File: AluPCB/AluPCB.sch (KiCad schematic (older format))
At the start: 83 parts, among them J1 CON_U, J2 CON_U, J3 CON_U, J4 GND, J5 VIN, Q1 AON6276, Q2 AON6276, Q3 AON6276, Q4 AON6276, Q5 AON6276, Q6 AON6276

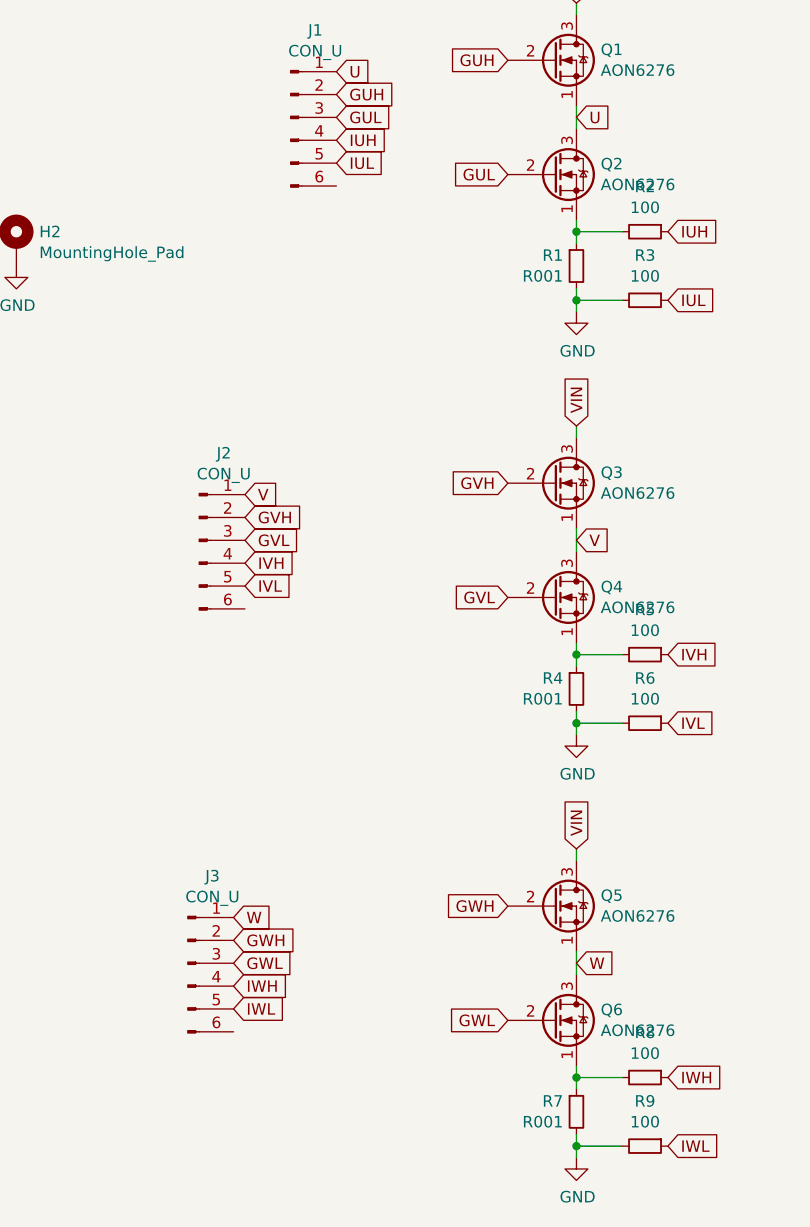
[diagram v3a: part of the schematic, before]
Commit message: finalized Powerstage, ordered PCBs
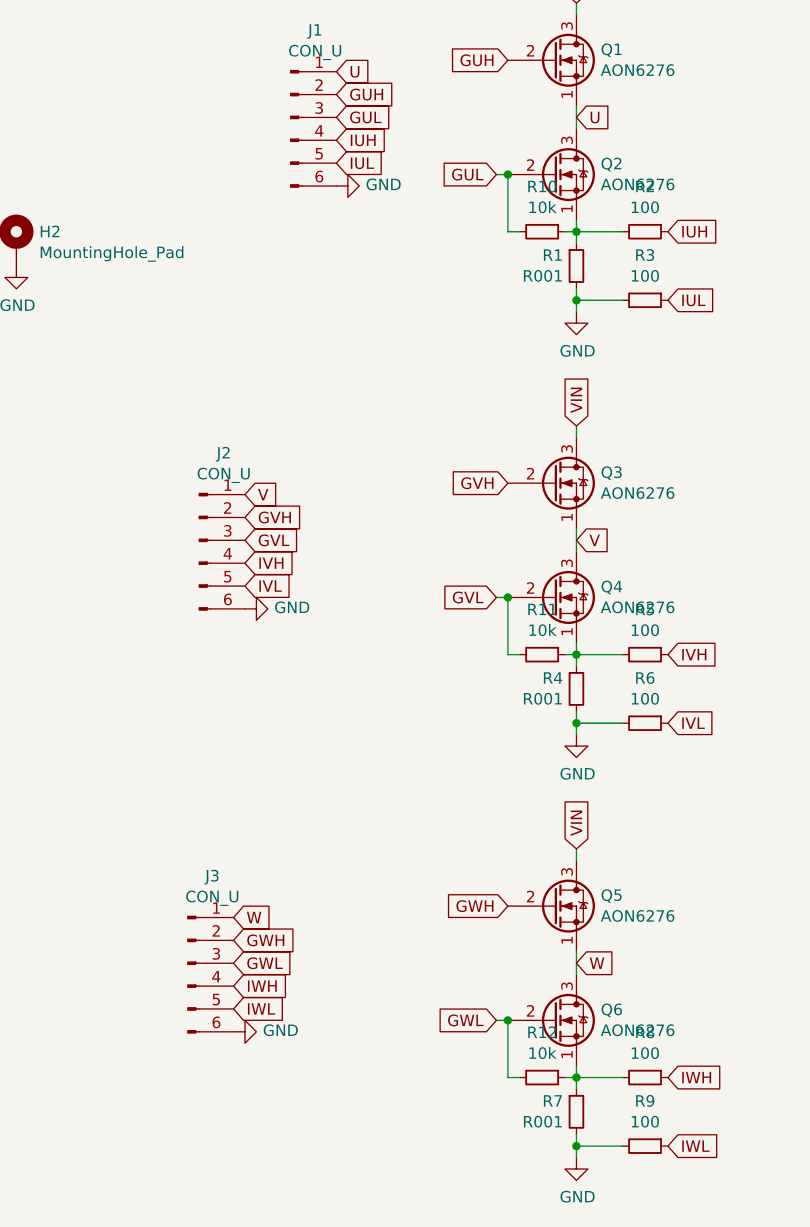
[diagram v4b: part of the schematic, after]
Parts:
- added R10, R11, R12: 10k, Resistor_SMD:R_0402_1005Metric, symbol Device:R_Small
- J1, J2, J3: footprint Connector_PinSocket_2.00mm:PinSocket_1x06_P2.00mm_Vertical_SMD_Pin1Left -> Connector_PinHeader_2.00mm:PinHeader_1x06_P2.00mm_Vertical_SMD_Pin1Left
- J4, J5: footprint Connector_PinSocket_2.00mm:PinSocket_1x03_P2.00mm_Vertical_SMD_Pin1Left -> Connector_PinHeader_2.00mm:PinHeader_1x03_P2.00mm_Vertical_SMD_Pin1Left
- R2, R3, R5, R6, R8, R9: footprint Resistor_SMD:R_0603_1608Metric -> Resistor_SMD:R_0402_1005Metric
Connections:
- net GND: now also J1.6 (Pin_6), J2.6 (Pin_6), J3.6 (Pin_6)
- net GUL: now also R10.2
- net GVL: now also R11.2
- net GWL: now also R12.2
- net at Q2.1 (S), R1.1, R2.2: now also R10.1
- net at Q4.1 (S), R4.1, R5.2: now also R11.1
- net at Q6.1 (S), R7.1, R8.2: now also R12.1
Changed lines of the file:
@@
 Text GLabel 3700 1250 0    50   Input ~ 0
 GUH
-Text GLabel 3700 1750 0    50   Input ~ 0
+Text GLabel 3650 1750 0    50   Input ~ 0
 GUL
 Text GLabel 4000 1500 2    50   Input ~ 0
@@
 F 0 "R2" V 4104 2000 50  0000 C CNN
 F 1 "100" V 4195 2000 50  0000 C CNN
-F 2 "Resistor_SMD:R_0603_1608Metric" H 4300 2000 50  0001 C CNN
+F 2 "Resistor_SMD:R_0402_1005Metric" H 4300 2000 50  0001 C CNN
 F 3 "~" H 4300 2000 50  0001 C CNN
 	1    4300 2000
@@
 F 0 "R3" V 4104 2300 50  0000 C CNN
 F 1 "100" V 4195 2300 50  0000 C CNN
-F 2 "Resistor_SMD:R_0603_1608Metric" H 4300 2300 50  0001 C CNN
+F 2 "Resistor_SMD:R_0402_1005Metric" H 4300 2300 50  0001 C CNN
 F 3 "~" H 4300 2300 50  0001 C CNN
 	1    4300 2300
@@
 F 0 "J1" H 2858 1881 50  0000 C CNN
 F 1 "CON_U" H 2858 1790 50  0000 C CNN
-F 2 "Connector_PinSocket_2.00mm:PinSocket_1x06_P2.00mm_Vertical_SMD_Pin1Left" H 2750 1500 50  0001 C CNN
+F 2 "Connector_PinHeader_2.00mm:PinHeader_1x06_P2.00mm_Vertical_SMD_Pin1Left" H 2750 1500 50  0001 C CNN
 F 3 "~" H 2750 1500 50  0001 C CNN
 	1    2750 1500
@@
 Text GLabel 3700 3100 0    50   Input ~ 0
 GVH
-Text GLabel 3700 3600 0    50   Input ~ 0
-GVL
 Text GLabel 4000 3350 2    50   Input ~ 0
 V
@@
 F 0 "R5" V 4104 3850 50  0000 C CNN
 F 1 "100" V 4195 3850 50  0000 C CNN
-F 2 "Resistor_SMD:R_0603_1608Metric" H 4300 3850 50  0001 C CNN
+F 2 "Resistor_SMD:R_0402_1005Metric" H 4300 3850 50  0001 C CNN
 F 3 "~" H 4300 3850 50  0001 C CNN
 	1    4300 3850
@@
 F 0 "R6" V 4104 4150 50  0000 C CNN
 F 1 "100" V 4195 4150 50  0000 C CNN
-F 2 "Resistor_SMD:R_0603_1608Metric" H 4300 4150 50  0001 C CNN
+F 2 "Resistor_SMD:R_0402_1005Metric" H 4300 4150 50  0001 C CNN
 F 3 "~" H 4300 4150 50  0001 C CNN
 	1    4300 4150
@@
 F 0 "J2" H 2458 3731 50  0000 C CNN
 F 1 "CON_U" H 2458 3640 50  0000 C CNN
-F 2 "Connector_PinSocket_2.00mm:PinSocket_1x06_P2.00mm_Vertical_SMD_Pin1Left" H 2350 3350 50  0001 C CNN
+F 2 "Connector_PinHeader_2.00mm:PinHeader_1x06_P2.00mm_Vertical_SMD_Pin1Left" H 2350 3350 50  0001 C CNN
 F 3 "~" H 2350 3350 50  0001 C CNN
 	1    2350 3350
@@
 Text GLabel 3700 4950 0    50   Input ~ 0
 GWH
-Text GLabel 3700 5450 0    50   Input ~ 0
+Text GLabel 3650 5450 0    50   Input ~ 0
 GWL
 Text GLabel 4000 5200 2    50   Input ~ 0
@@
 F 0 "R8" V 4104 5700 50  0000 C CNN
 F 1 "100" V 4195 5700 50  0000 C CNN
-F 2 "Resistor_SMD:R_0603_1608Metric" H 4300 5700 50  0001 C CNN
+F 2 "Resistor_SMD:R_0402_1005Metric" H 4300 5700 50  0001 C CNN
 F 3 "~" H 4300 5700 50  0001 C CNN
 	1    4300 5700
@@
 F 0 "R9" V 4104 6000 50  0000 C CNN
 F 1 "100" V 4195 6000 50  0000 C CNN
-F 2 "Resistor_SMD:R_0603_1608Metric" H 4300 6000 50  0001 C CNN
+F 2 "Resistor_SMD:R_0402_1005Metric" H 4300 6000 50  0001 C CNN
 F 3 "~" H 4300 6000 50  0001 C CNN
 	1    4300 6000
@@
 F 0 "J3" H 2408 5581 50  0000 C CNN
 F 1 "CON_U" H 2408 5490 50  0000 C CNN
-F 2 "Connector_PinSocket_2.00mm:PinSocket_1x06_P2.00mm_Vertical_SMD_Pin1Left" H 2300 5200 50  0001 C CNN
+F 2 "Connector_PinHeader_2.00mm:PinHeader_1x06_P2.00mm_Vertical_SMD_Pin1Left" H 2300 5200 50  0001 C CNN
 F 3 "~" H 2300 5200 50  0001 C CNN
 	1    2300 5200
@@
 F 0 "J4" H 858 3481 50  0000 C CNN
 F 1 "GND" H 858 3390 50  0000 C CNN
-F 2 "Connector_PinSocket_2.00mm:PinSocket_1x03_P2.00mm_Vertical_SMD_Pin1Left" H 750 3200 50  0001 C CNN
+F 2 "Connector_PinHeader_2.00mm:PinHeader_1x03_P2.00mm_Vertical_SMD_Pin1Left" H 750 3200 50  0001 C CNN
 F 3 "~" H 750 3200 50  0001 C CNN
 	1    750  3200
@@
 F 0 "J5" H 858 4031 50  0000 C CNN
 F 1 "VIN" H 858 3940 50  0000 C CNN
-F 2 "Connector_PinSocket_2.00mm:PinSocket_1x03_P2.00mm_Vertical_SMD_Pin1Left" H 750 3750 50  0001 C CNN
+F 2 "Connector_PinHeader_2.00mm:PinHeader_1x03_P2.00mm_Vertical_SMD_Pin1Left" H 750 3750 50  0001 C CNN
 F 3 "~" H 750 3750 50  0001 C CNN
 	1    750  3750
 	1    0    0    -1
 $EndComp
+$Comp
+L Device:R_Small R11
+U 1 1 5CD1A975
+P 3850 3850
+F 0 "R11" V 3654 3850 50  0000 C CNN
+F 1 "10k" V 3745 3850 50  0000 C CNN
+F 2 "Resistor_SMD:R_0402_1005Metric" H 3850 3850 50  0001 C CNN
+F 3 "~" H 3850 3850 50  0001 C CNN
+	1    3850 3850
+	0    1    1    0
+$EndComp
+Text GLabel 3650 3600 0    50   Input ~ 0
+GVL
+Wire Wire Line
+	3950 3850 4000 3850
+Wire Wire Line
+	3750 3850 3700 3850
+Wire Wire Line
+	3700 3850 3700 3600
+Wire Wire Line
+	3650 3600 3700 3600
+Connection ~ 3700 3600
+$Comp
+L Device:R_Small R10
+U 1 1 5CD24169
+P 3850 2000
+F 0 "R10" V 3654 2000 50  0000 C CNN
+F 1 "10k" V 3745 2000 50  0000 C CNN
+F 2 "Resistor_SMD:R_0402_1005Metric" H 3850 2000 50  0001 C CNN
+F 3 "~" H 3850 2000 50  0001 C CNN
+	1    3850 2000
+	0    1    1    0
+$EndComp
+Wire Wire Line
+	3650 1750 3700 1750
+Wire Wire Line
+	3700 1750 3700 2000
+Wire Wire Line
+	3700 2000 3750 2000
+Connection ~ 3700 1750
+Wire Wire Line
+	3950 2000 4000 2000
+$Comp
+L Device:R_Small R12
+U 1 1 5CD2793A
+P 3850 5700
+F 0 "R12" V 3654 5700 50  0000 C CNN
+F 1 "10k" V 3745 5700 50  0000 C CNN
+F 2 "Resistor_SMD:R_0402_1005Metric" H 3850 5700 50  0001 C CNN
+F 3 "~" H 3850 5700 50  0001 C CNN
+	1    3850 5700
+	0    1    1    0
+$EndComp
+Wire Wire Line
+	3650 5450 3700 5450
+Wire Wire Line
+	3700 5450 3700 5700
+Wire Wire Line
+	3700 5700 3750 5700
+Connection ~ 3700 5450
+Wire Wire Line
+	3950 5700 4000 5700
+$Comp
+L power:GND #PWR?
+U 1 1 5CDADC4B
+P 2500 5500
+F 0 "#PWR?" H 2500 5250 50  0001 C CNN
+F 1 "GND" V 2505 5372 50  0000 R CNN
+F 2 "" H 2500 5500 50  0001 C CNN
+F 3 "" H 2500 5500 50  0001 C CNN
+	1    2500 5500
+	0    -1   -1   0
+$EndComp
+$Comp
+L power:GND #PWR?
+U 1 1 5CDAEC29
+P 2550 3650
+F 0 "#PWR?" H 2550 3400 50  0001 C CNN
+F 1 "GND" V 2555 3522 50  0000 R CNN
+F 2 "" H 2550 3650 50  0001 C CNN
+F 3 "" H 2550 3650 50  0001 C CNN
+	1    2550 3650
+	0    -1   -1   0
+$EndComp
+$Comp
+L power:GND #PWR?
+U 1 1 5CDAFC32
+P 2950 1800
+F 0 "#PWR?" H 2950 1550 50  0001 C CNN
+F 1 "GND" V 2955 1672 50  0000 R CNN
+F 2 "" H 2950 1800 50  0001 C CNN
+F 3 "" H 2950 1800 50  0001 C CNN
+	1    2950 1800
+	0    -1   -1   0
+$EndComp
 $EndSCHEMATC

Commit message: added gerber
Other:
- note added: "NTMFS6H800N 80V 203A 2.3mOhm 4.99€\nNTMFS6B03N 100V 132A 4.8mOhm 5.77€\nAON6276 80V 100A 2.6mOhm 0.8€"
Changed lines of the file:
@@
 	0    -1   -1   0
 $EndComp
+Text Notes 4250 850  0    50   ~ 0
+NTMFS6H800N 80V 203A 2.3mOhm 4.99€\nNTMFS6B03N 100V 132A 4.8mOhm 5.77€\nAON6276 80V 100A 2.6mOhm 0.8€
 $EndSCHEMATC
